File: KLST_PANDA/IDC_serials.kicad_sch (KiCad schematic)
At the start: 0 parts

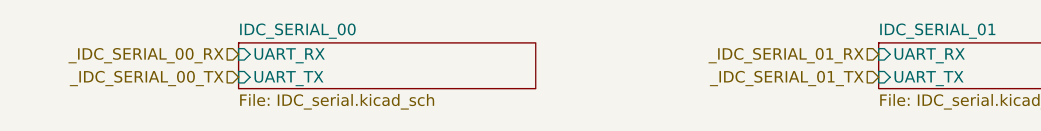
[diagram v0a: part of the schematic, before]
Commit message: added MIDI analog, I2C and buttons
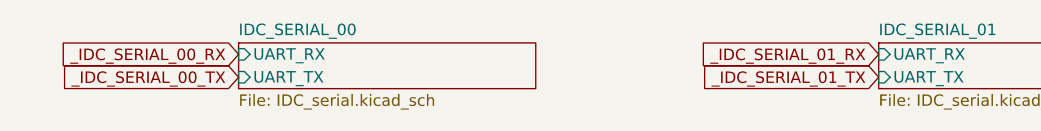
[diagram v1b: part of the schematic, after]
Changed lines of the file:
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@@
 (kicad_sch (version 20230121) (generator eeschema)
   (paper "A4")
-  (hierarchical_label "_IDC_SERIAL_00_TX" (shape input) (at 107.95 102.87 180) (fields_autoplaced)
+  (global_label "_IDC_SERIAL_00_TX" (shape input) (at 107.95 102.87 180) (fields_autoplaced)
     (effects (font (size 1.27 1.27)) (justify right))
+    (property "Intersheetrefs" "${INTERSHEET_REFS}" (at 87.0829 102.87 0)
+      (effects (font (size 1.27 1.27)) (justify right) hide)
+    )
   )
-  (hierarchical_label "_IDC_SERIAL_01_RX" (shape input) (at 179.07 100.33 180) (fields_autoplaced)
+  (global_label "_IDC_SERIAL_01_TX" (shape input) (at 179.07 102.87 180) (fields_autoplaced)
     (effects (font (size 1.27 1.27)) (justify right))
+    (property "Intersheetrefs" "${INTERSHEET_REFS}" (at 158.2029 102.87 0)
+      (effects (font (size 1.27 1.27)) (justify right) hide)
+    )
   )
-  (hierarchical_label "_IDC_SERIAL_00_RX" (shape input) (at 107.95 100.33 180) (fields_autoplaced)
+  (global_label "_IDC_SERIAL_00_RX" (shape input) (at 107.95 100.33 180) (fields_autoplaced)
     (effects (font (size 1.27 1.27)) (justify right))
+    (property "Intersheetrefs" "${INTERSHEET_REFS}" (at 86.7805 100.33 0)
+      (effects (font (size 1.27 1.27)) (justify right) hide)
+    )
   )
-  (hierarchical_label "_IDC_SERIAL_01_TX" (shape input) (at 179.07 102.87 180) (fields_autoplaced)
+  (global_label "_IDC_SERIAL_01_RX" (shape input) (at 179.07 100.33 180) (fields_autoplaced)
     (effects (font (size 1.27 1.27)) (justify right))
+    (property "Intersheetrefs" "${INTERSHEET_REFS}" (at 157.9005 100.33 0)
+      (effects (font (size 1.27 1.27)) (justify right) hide)
+    )
   )
   (sheet (at 107.95 99.06) (size 33.02 5.08) (fields_autoplaced)

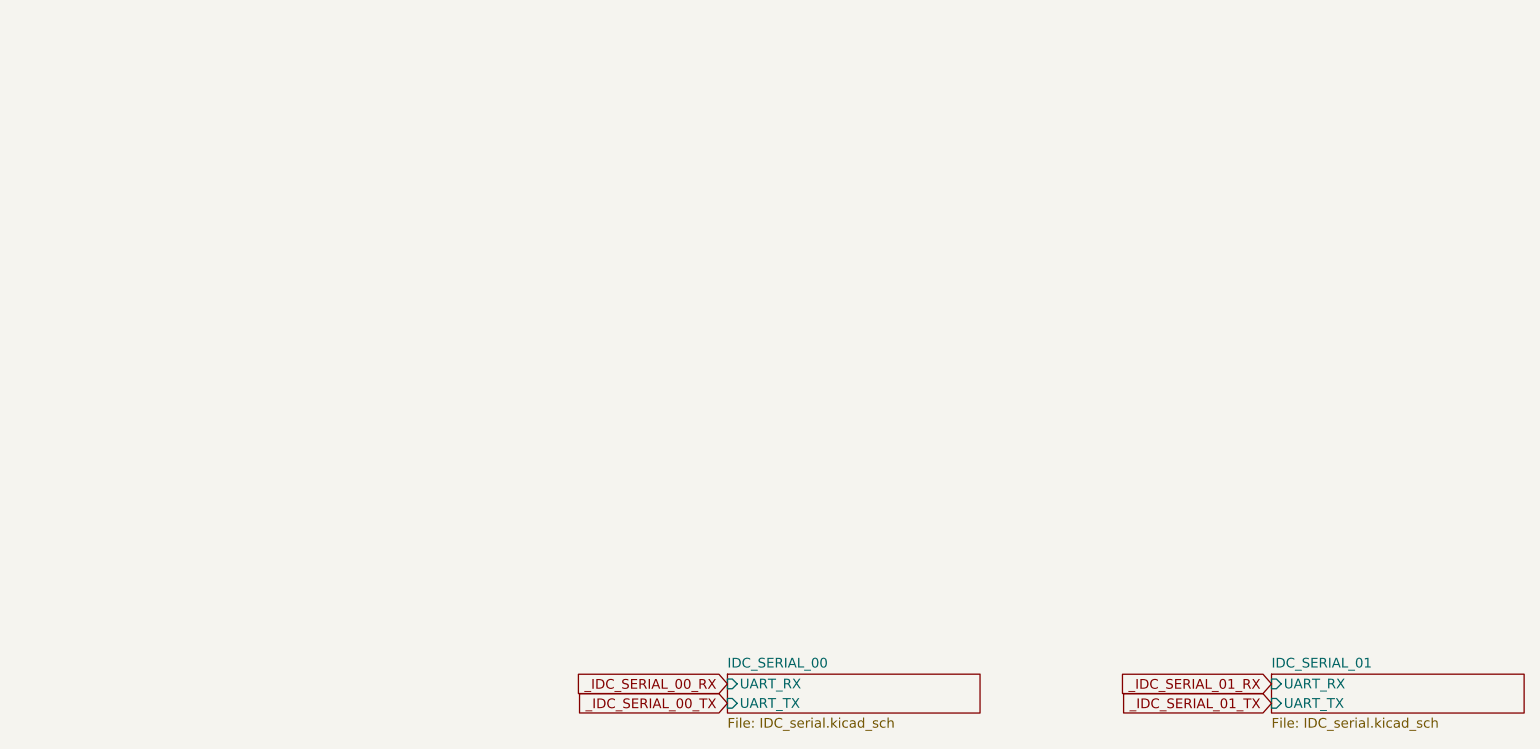
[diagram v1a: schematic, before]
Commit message: moved core (MCU) to sheet, cleaned up sheets
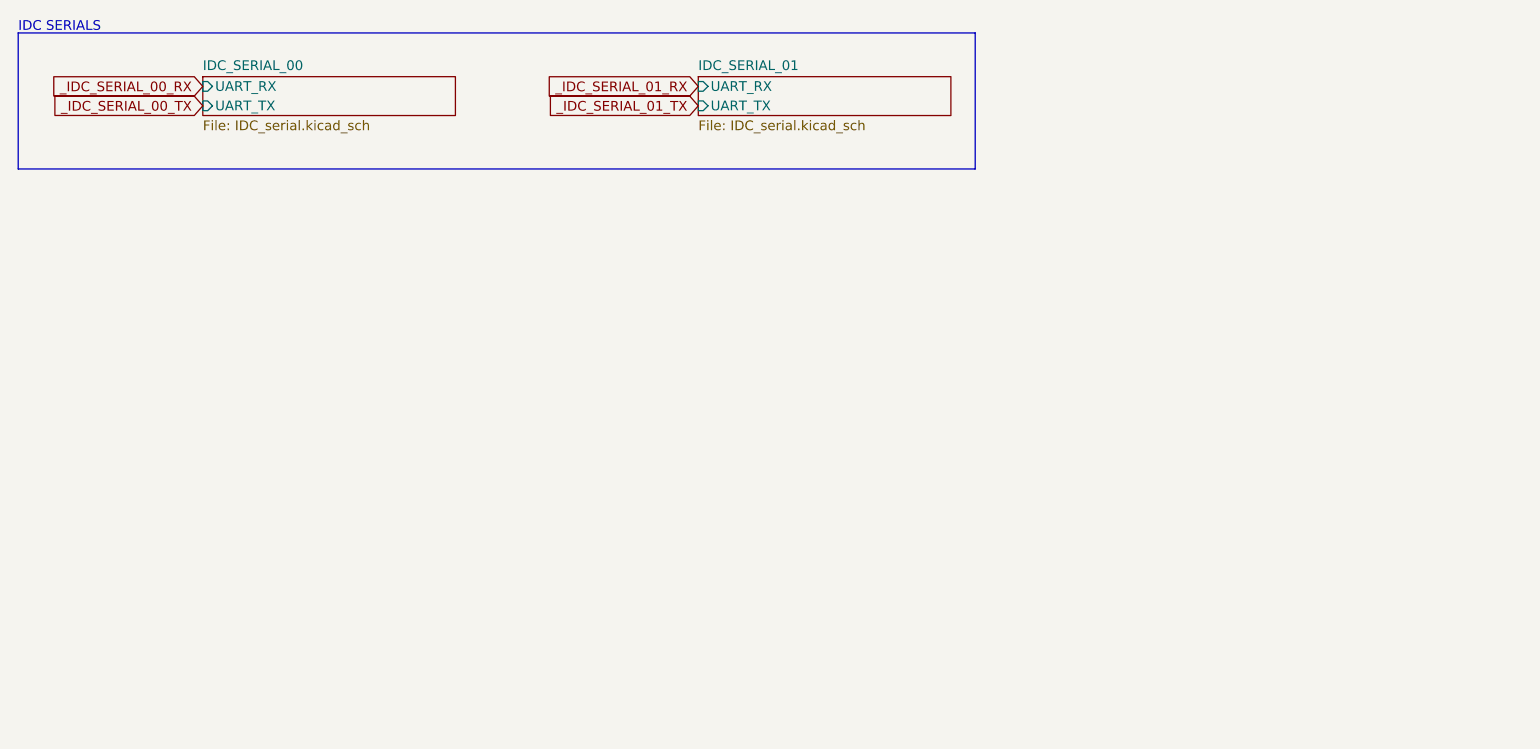
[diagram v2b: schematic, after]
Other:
- note added: "IDC SERIALS"
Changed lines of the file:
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@@
 (kicad_sch (version 20230121) (generator eeschema)
   (paper "A4")
-  (global_label "_IDC_SERIAL_00_TX" (shape input) (at 107.95 102.87 180) (fields_autoplaced)
+  (rectangle (start 15.24 15.24) (end 140.335 33.02)
+    (stroke (width 0) (type default))
+    (fill (type none))
+  )
+  (text "IDC SERIALS" (at 15.24 15.24 0)
+    (effects (font (size 1.27 1.27)) (justify left bottom))
+  )
+  (global_label "_IDC_SERIAL_00_TX" (shape input) (at 39.37 24.765 180) (fields_autoplaced)
     (effects (font (size 1.27 1.27)) (justify right))
-    (property "Intersheetrefs" "${INTERSHEET_REFS}" (at 87.0829 102.87 0)
+    (property "Intersheetrefs" "${INTERSHEET_REFS}" (at 18.5029 24.765 0)
       (effects (font (size 1.27 1.27)) (justify right) hide)
     )
   )
-  (global_label "_IDC_SERIAL_01_TX" (shape input) (at 179.07 102.87 180) (fields_autoplaced)
+  (global_label "_IDC_SERIAL_01_TX" (shape input) (at 104.14 24.765 180) (fields_autoplaced)
     (effects (font (size 1.27 1.27)) (justify right))
-    (property "Intersheetrefs" "${INTERSHEET_REFS}" (at 158.2029 102.87 0)
+    (property "Intersheetrefs" "${INTERSHEET_REFS}" (at 83.2729 24.765 0)
       (effects (font (size 1.27 1.27)) (justify right) hide)
     )
   )
-  (global_label "_IDC_SERIAL_00_RX" (shape input) (at 107.95 100.33 180) (fields_autoplaced)
+  (global_label "_IDC_SERIAL_00_RX" (shape input) (at 39.37 22.225 180) (fields_autoplaced)
     (effects (font (size 1.27 1.27)) (justify right))
-    (property "Intersheetrefs" "${INTERSHEET_REFS}" (at 86.7805 100.33 0)
+    (property "Intersheetrefs" "${INTERSHEET_REFS}" (at 18.2005 22.225 0)
       (effects (font (size 1.27 1.27)) (justify right) hide)
     )
   )
-  (global_label "_IDC_SERIAL_01_RX" (shape input) (at 179.07 100.33 180) (fields_autoplaced)
+  (global_label "_IDC_SERIAL_01_RX" (shape input) (at 104.14 22.225 180) (fields_autoplaced)
     (effects (font (size 1.27 1.27)) (justify right))
-    (property "Intersheetrefs" "${INTERSHEET_REFS}" (at 157.9005 100.33 0)
+    (property "Intersheetrefs" "${INTERSHEET_REFS}" (at 82.9705 22.225 0)
       (effects (font (size 1.27 1.27)) (justify right) hide)
     )
   )
-  (sheet (at 107.95 99.06) (size 33.02 5.08) (fields_autoplaced)
+  (sheet (at 39.37 20.955) (size 33.02 5.08) (fields_autoplaced)
     (stroke (width 0.1524) (type solid))
     (fill (color 0 0 0 0.0000))
-    (property "Sheetname" "IDC_SERIAL_00" (at 107.95 98.3484 0)
+    (property "Sheetname" "IDC_SERIAL_00" (at 39.37 20.2434 0)
       (effects (font (size 1.27 1.27)) (justify left bottom))
     )
-    (property "Sheetfile" "IDC_serial.kicad_sch" (at 107.95 104.7246 0)
+    (property "Sheetfile" "IDC_serial.kicad_sch" (at 39.37 26.6196 0)
       (effects (font (size 1.27 1.27)) (justify left top))
     )
-    (pin "UART_RX" input (at 107.95 100.33 180)
+    (pin "UART_RX" input (at 39.37 22.225 180)
       (effects (font (size 1.27 1.27)) (justify left))
     )
-    (pin "UART_TX" input (at 107.95 102.87 180)
+    (pin "UART_TX" input (at 39.37 24.765 180)
       (effects (font (size 1.27 1.27)) (justify left))
     )
@@
     )
   )
-  (sheet (at 179.07 99.06) (size 33.02 5.08) (fields_autoplaced)
+  (sheet (at 104.14 20.955) (size 33.02 5.08) (fields_autoplaced)
     (stroke (width 0.1524) (type solid))
     (fill (color 0 0 0 0.0000))
-    (property "Sheetname" "IDC_SERIAL_01" (at 179.07 98.3484 0)
+    (property "Sheetname" "IDC_SERIAL_01" (at 104.14 20.2434 0)
       (effects (font (size 1.27 1.27)) (justify left bottom))
     )
-    (property "Sheetfile" "IDC_serial.kicad_sch" (at 179.07 104.7246 0)
+    (property "Sheetfile" "IDC_serial.kicad_sch" (at 104.14 26.6196 0)
       (effects (font (size 1.27 1.27)) (justify left top))
     )
-    (pin "UART_RX" input (at 179.07 100.33 180)
+    (pin "UART_RX" input (at 104.14 22.225 180)
       (effects (font (size 1.27 1.27)) (justify left))
     )
-    (pin "UART_TX" input (at 179.07 102.87 180)
+    (pin "UART_TX" input (at 104.14 24.765 180)
       (effects (font (size 1.27 1.27)) (justify left))
     )

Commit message: continued routing
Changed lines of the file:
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@@
     (effects (font (size 1.27 1.27)) (justify left bottom))
   )
-  (global_label "_IDC_SERIAL_00_TX" (shape input) (at 39.37 24.765 180) (fields_autoplaced)
+  (global_label "_IDC_SERIAL_00_TX" (shape input) (at 104.14 24.765 180) (fields_autoplaced)
+    (effects (font (size 1.27 1.27)) (justify right))
+    (property "Intersheetrefs" "${INTERSHEET_REFS}" (at 83.2729 24.765 0)
+      (effects (font (size 1.27 1.27)) (justify right) hide)
+    )
+  )
+  (global_label "_IDC_SERIAL_01_TX" (shape input) (at 39.37 24.765 180) (fields_autoplaced)
     (effects (font (size 1.27 1.27)) (justify right))
     (property "Intersheetrefs" "${INTERSHEET_REFS}" (at 18.5029 24.765 0)
@@
     )
   )
-  (global_label "_IDC_SERIAL_01_TX" (shape input) (at 104.14 24.765 180) (fields_autoplaced)
+  (global_label "_IDC_SERIAL_00_RX" (shape input) (at 104.14 22.225 180) (fields_autoplaced)
     (effects (font (size 1.27 1.27)) (justify right))
-    (property "Intersheetrefs" "${INTERSHEET_REFS}" (at 83.2729 24.765 0)
+    (property "Intersheetrefs" "${INTERSHEET_REFS}" (at 82.9705 22.225 0)
       (effects (font (size 1.27 1.27)) (justify right) hide)
     )
   )
-  (global_label "_IDC_SERIAL_00_RX" (shape input) (at 39.37 22.225 180) (fields_autoplaced)
+  (global_label "_IDC_SERIAL_01_RX" (shape input) (at 39.37 22.225 180) (fields_autoplaced)
     (effects (font (size 1.27 1.27)) (justify right))
     (property "Intersheetrefs" "${INTERSHEET_REFS}" (at 18.2005 22.225 0)
       (effects (font (size 1.27 1.27)) (justify right) hide)
     )
-  )
-  (global_label "_IDC_SERIAL_01_RX" (shape input) (at 104.14 22.225 180) (fields_autoplaced)
-    (effects (font (size 1.27 1.27)) (justify right))
-    (property "Intersheetrefs" "${INTERSHEET_REFS}" (at 82.9705 22.225 0)
-      (effects (font (size 1.27 1.27)) (justify right) hide)
-    )
